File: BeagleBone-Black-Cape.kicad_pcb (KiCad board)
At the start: 4 copper layers, 61.9 x 92.1 mm, 77 parts, among them J501 Conn_ARM_JTAG_SWD_10, J502 3.3V, P101 BeagleBone_Black_Header, P102 BeagleBone_Black_Header, U401 LM3671, U601 cc1352p, U602 MX25R8035FZUIL0, Y601 32.768kHz, Y602 48MHz

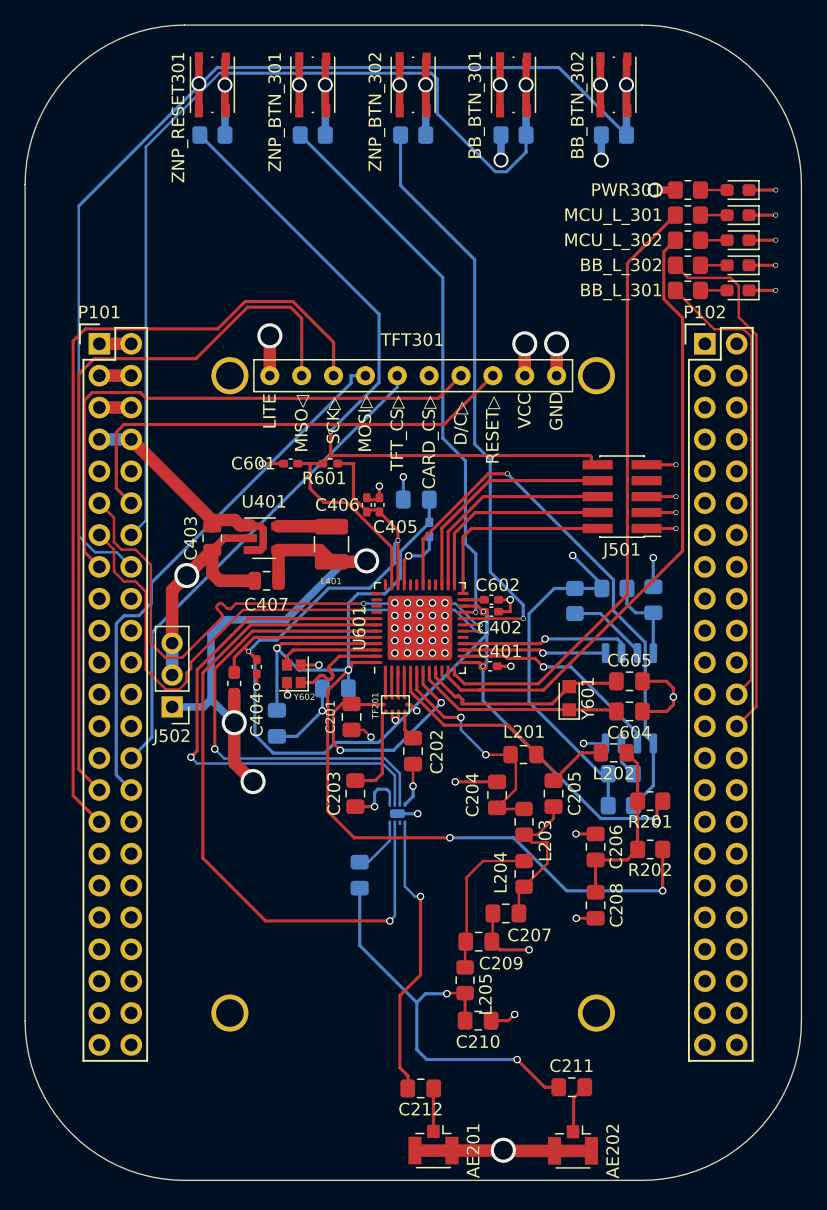
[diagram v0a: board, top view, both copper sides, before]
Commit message: via conversion complete
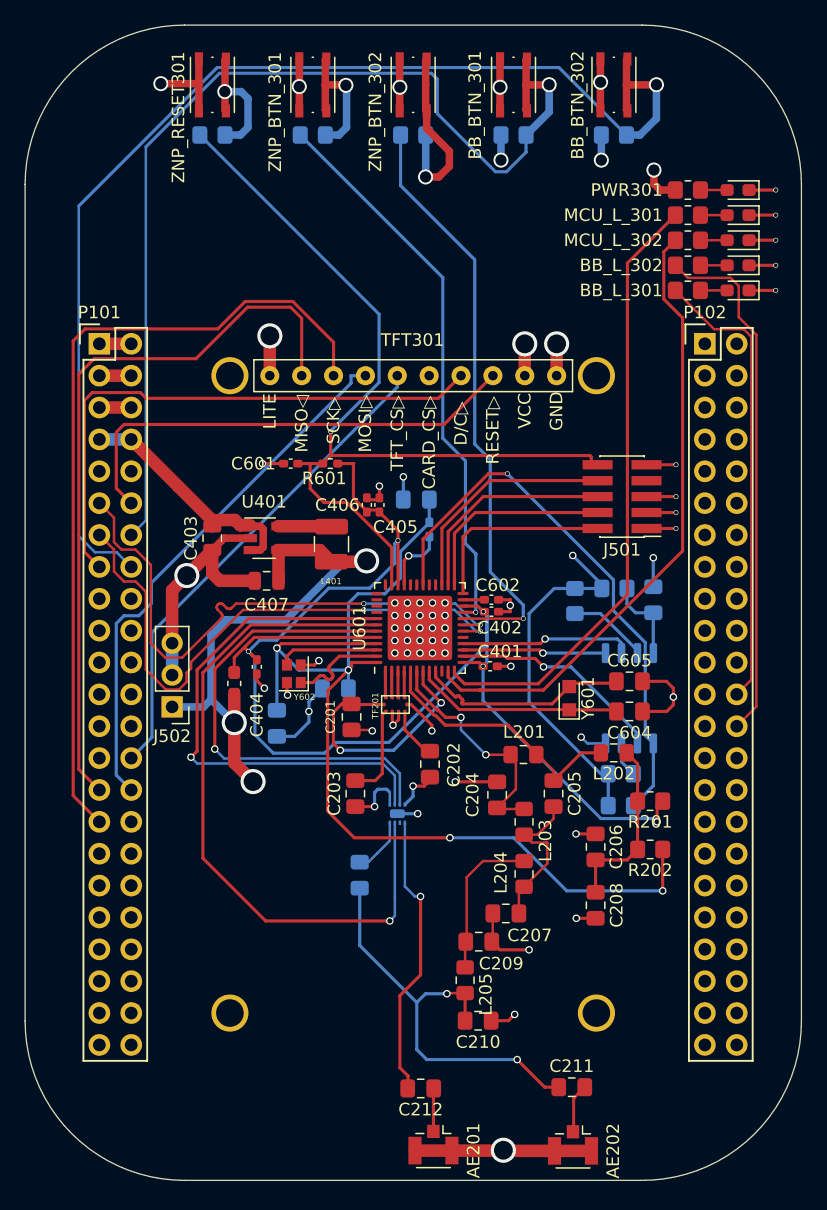
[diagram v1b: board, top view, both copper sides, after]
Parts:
- moved C202 1.70 mm to (142.7, 95.9)
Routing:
- net Net-(R305-Pad1): track 8.19 -> 15.0 mm
- net GND: track 142.6 -> 148.9 mm
- net BB_BTN_2: track 90.1 -> 94.2 mm
- net Net-(R304-Pad1): track 8.19 -> 11.2 mm
- net BB_BTN_1: track 79.2 -> 81.8 mm
- net Net-(R302-Pad1): track 8.18 -> 10.7 mm
- net Net-(C202-Pad2): track 2.42 -> 4.20 mm
- net MCU_VDD: track 85.6 -> 87.0 mm

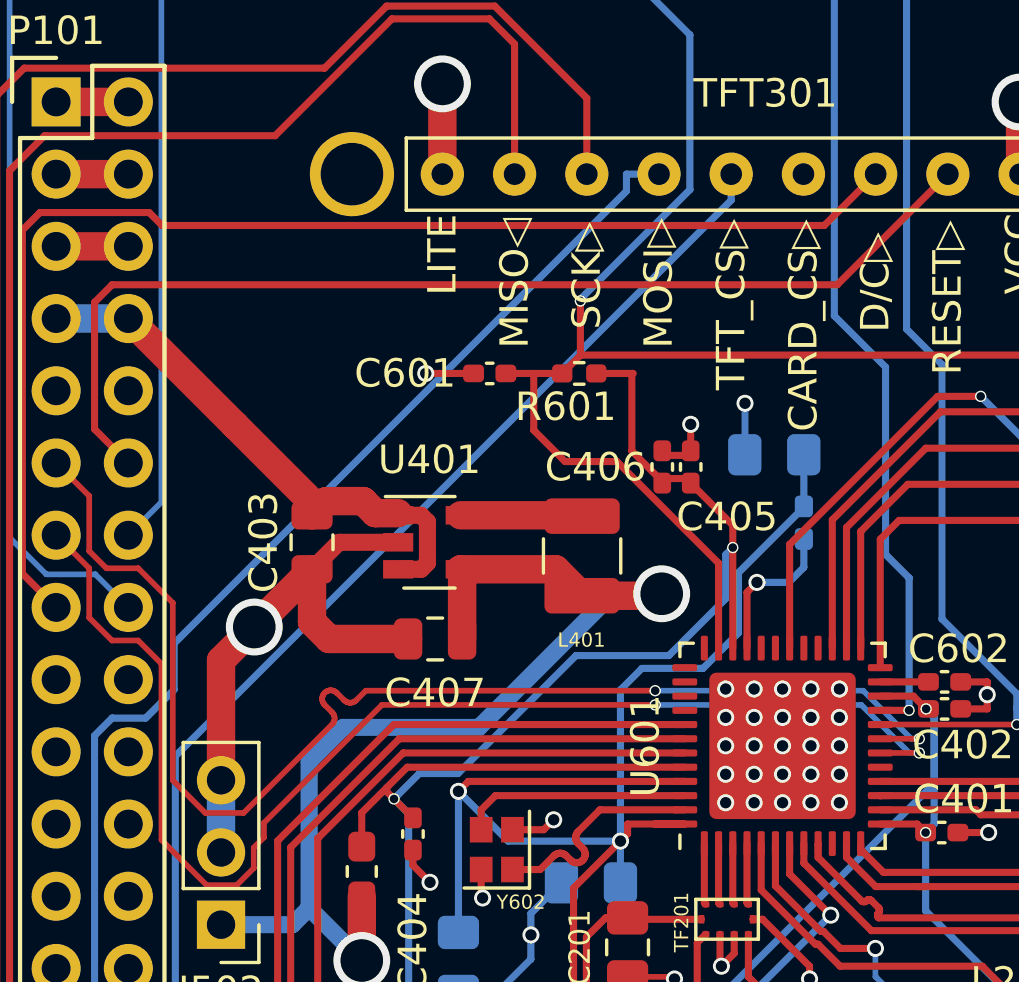
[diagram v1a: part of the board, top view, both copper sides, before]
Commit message: filling around new through vias complete. need reviews. onto zach for LCD holes and index dots
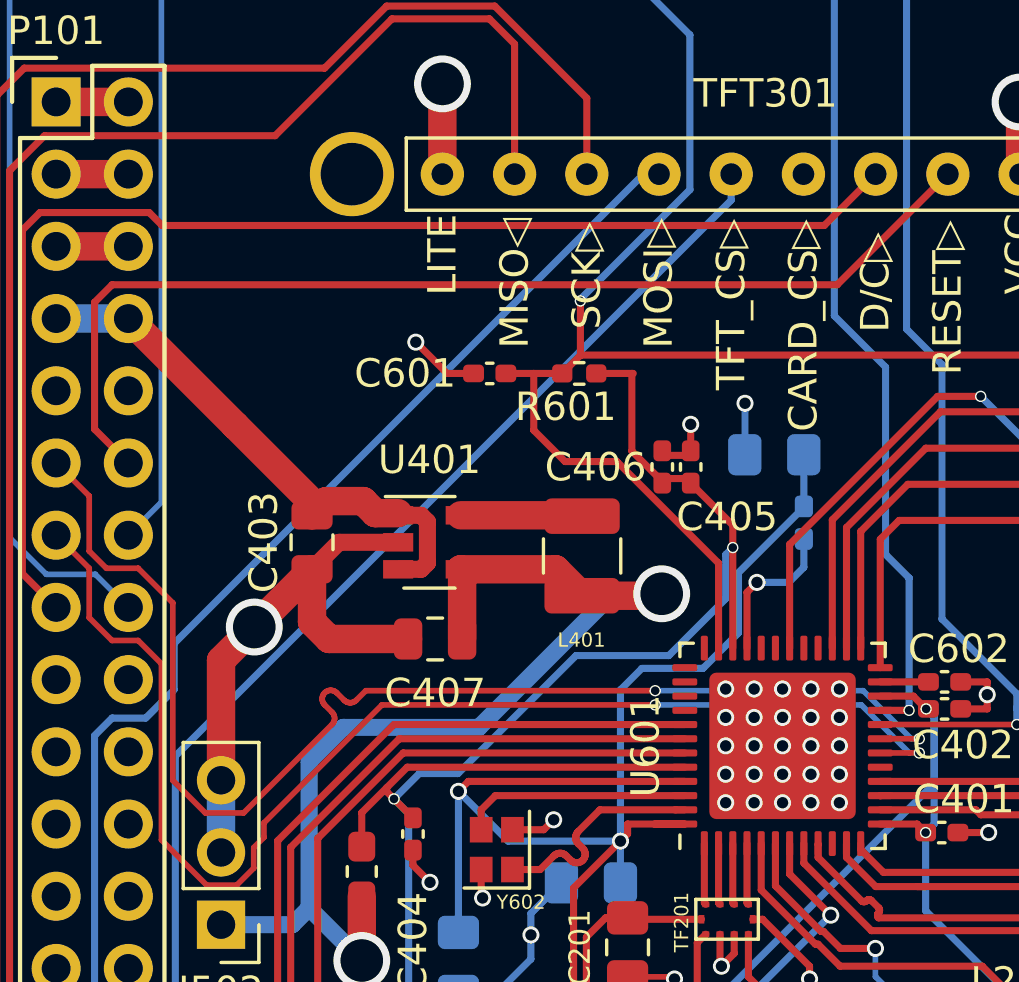
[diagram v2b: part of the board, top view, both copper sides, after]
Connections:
- AE201 pad 2: (no net) -> GND
- AE202 pad 2: (no net) -> GND
- P101 pad 11: ZNP_TX -> GND
- U601 pad 19: ZNP_TX -> GND
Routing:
- net GND: track 148.9 -> 209.4 mm, vias 60 -> 63
- net ZNP_TX: track 45.5 -> 0.00 mm, vias 2 -> 0
- net (no net): track 15.1 -> 1.02 mm, vias 2 -> 1

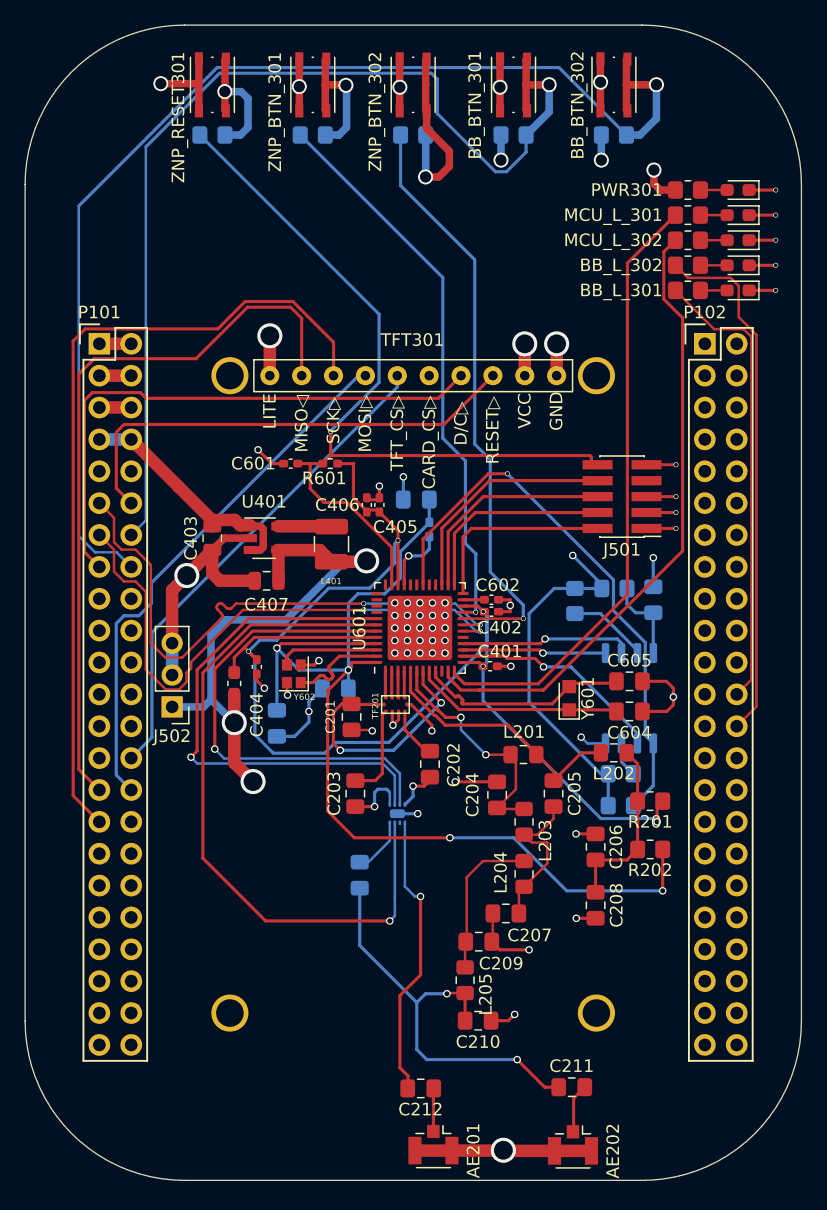
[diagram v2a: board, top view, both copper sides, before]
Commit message: updated footprint, updated some traces, added indexing dots
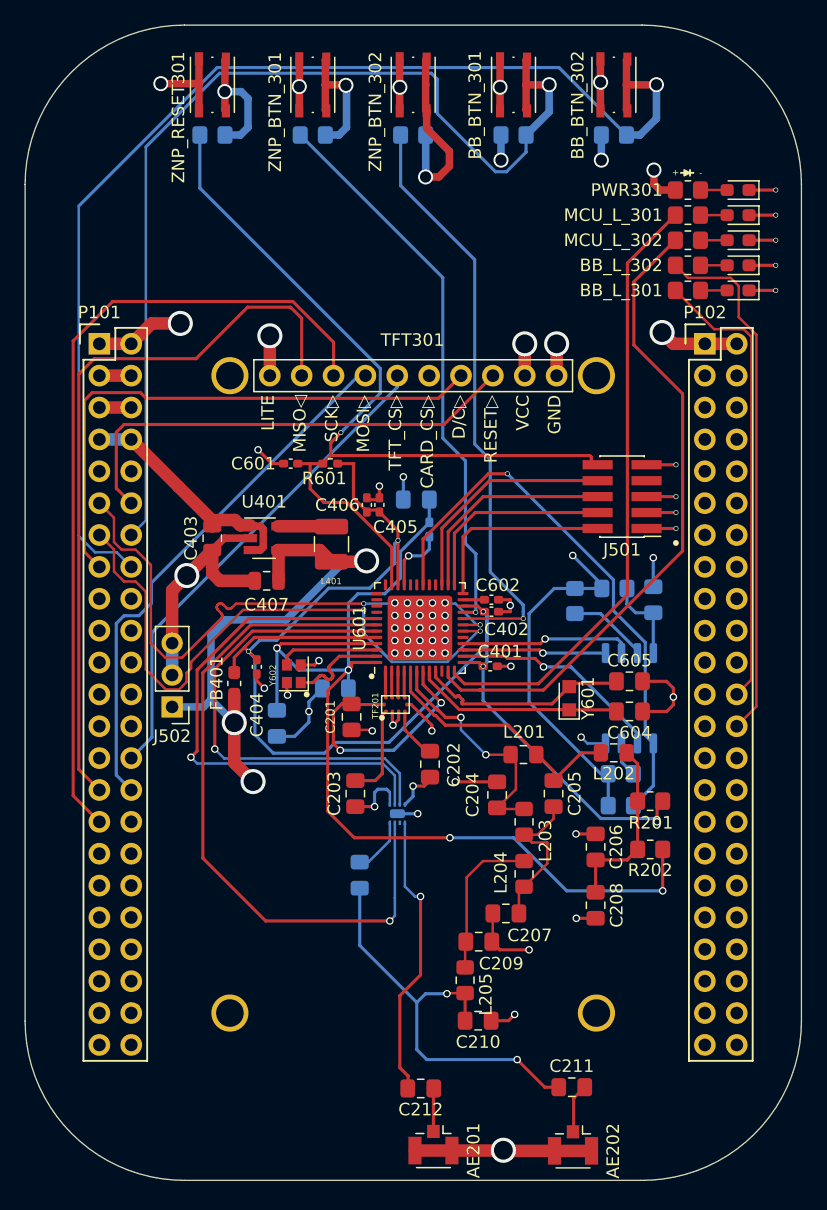
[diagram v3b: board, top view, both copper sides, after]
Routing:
- net GND: track 209.4 -> 220.3 mm, vias 63 -> 65
- net ZNP_RX: track 45.5 -> 48.6 mm
- net MCU_LED_2: track 50.3 -> 52.2 mm
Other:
- board text added: "+"
- board text added: "-"

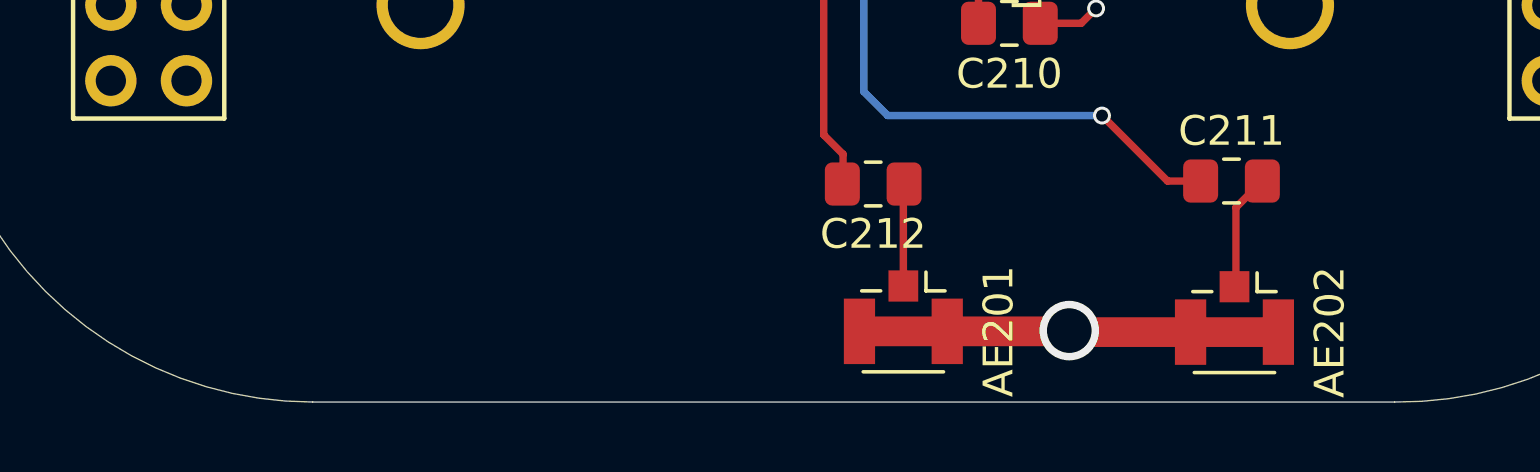
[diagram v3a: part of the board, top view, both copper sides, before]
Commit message: added silkscreen with board name and revision number
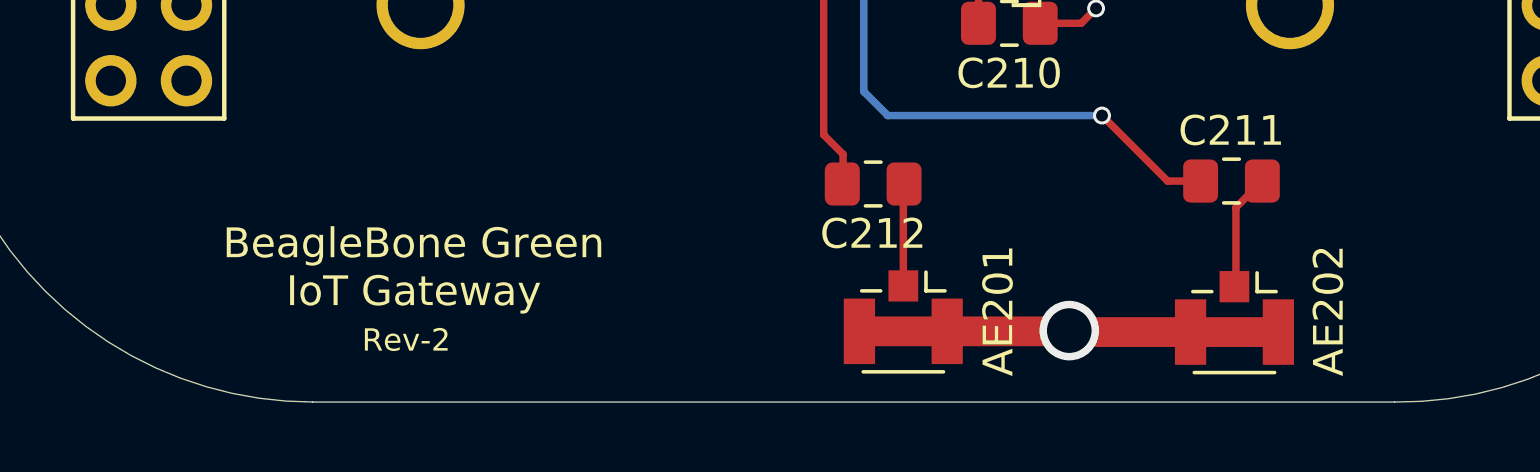
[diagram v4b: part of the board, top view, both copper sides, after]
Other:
- board text added: "BeagleBone Green IoT Gateway"
- board text added: "Rev-2"
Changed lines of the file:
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@@
   (general
     (thickness 1.6)
-    (drawings 20)
+    (drawings 22)
     (tracks 855)
     (zones 0)
@@
     (0 F.Cu signal)
     (1 GNDP.Cu power hide)
-    (2 PWRP.Cu power hide)
+    (2 PWRP.Cu power)
     (31 B.Cu signal)
     (32 B.Adhes user)
@@
     (tags "Hirose U.FL Coaxial")
     (attr smd)
-    (fp_text reference AE201 (at 0.475 -3.2 90) (layer F.SilkS)
+    (fp_text reference AE201 (at -0.225 -3.2 90) (layer F.SilkS)
       (effects (font (size 1 1) (thickness 0.15)))
     )
@@
     (tags "Hirose U.FL Coaxial")
     (attr smd)
-    (fp_text reference AE202 (at 0.475 -3.2 90) (layer F.SilkS)
+    (fp_text reference AE202 (at -0.25 -3.175 90) (layer F.SilkS)
       (effects (font (size 1 1) (thickness 0.15)))
     )
@@
     )
   )
+  (gr_text Rev-2 (at 126.2951 126.9824) (layer F.SilkS)
+    (effects (font (size 0.75 0.75) (thickness 0.1875)))
+  )
+  (gr_text "BeagleBone Green \nIoT Gateway" (at 126.5451 124.5324) (layer F.SilkS)
+    (effects (font (size 1 1) (thickness 0.25)))
+  )
   (gr_text - (at 164.2951 48.7574) (layer F.SilkS)

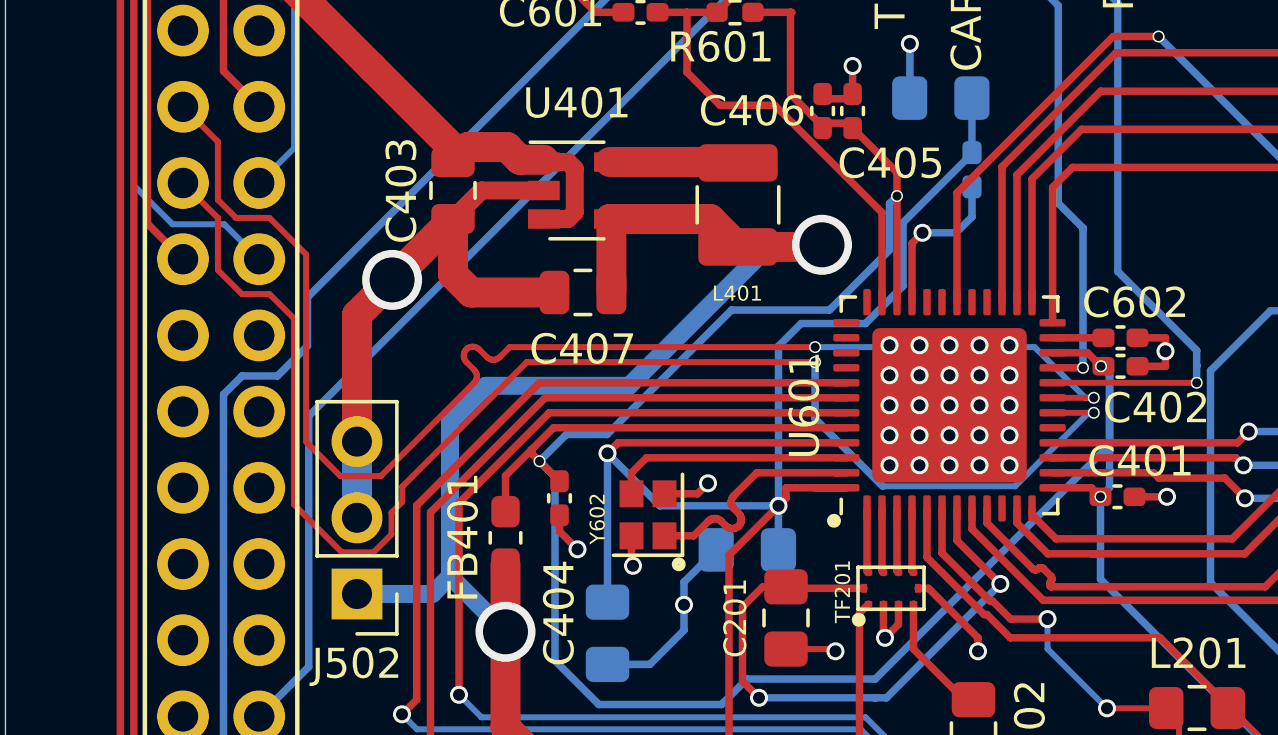
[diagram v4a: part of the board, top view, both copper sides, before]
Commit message: Fixed U601 p19 being connected to GND net instead of ZNP_TX
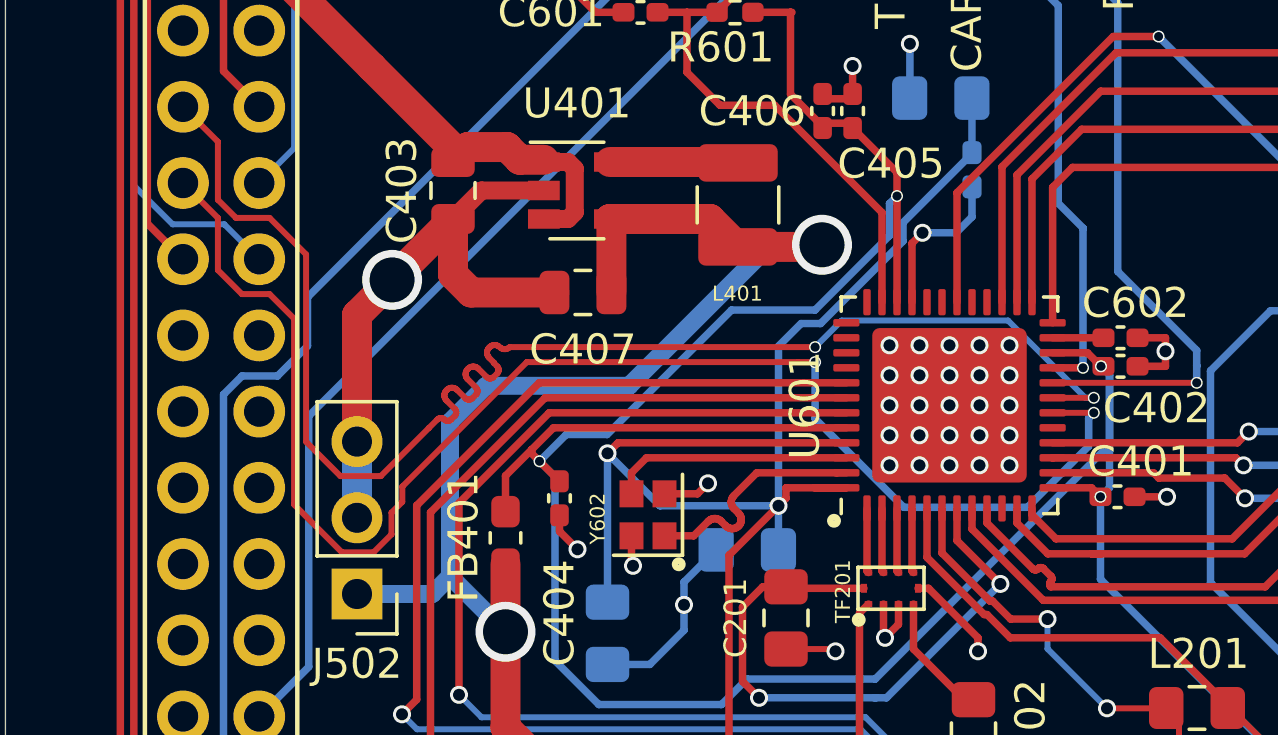
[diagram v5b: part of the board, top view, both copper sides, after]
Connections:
- AE201 pad 2: GND -> (no net)
- AE202 pad 2: GND -> (no net)
- P101 pad 11: GND -> ZNP_TX
- U601 pad 19: GND -> ZNP_TX
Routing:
- net GND: track 220.3 -> 160.6 mm, vias 65 -> 62
- net ZNP_TX: track 0.00 -> 48.4 mm, vias 0 -> 2
- net (no net): track 1.02 -> 15.1 mm, vias 1 -> 2
- net ZNP_RX: track 48.6 -> 49.8 mm
- net VDDR: track 86.8 -> 86.0 mm
